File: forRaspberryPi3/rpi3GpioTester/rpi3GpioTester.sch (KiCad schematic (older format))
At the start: 59 parts, among them J1 Raspberry_Pi_2_3, J2 Conn_01x20_Male, J3 Conn_01x12_Male, SW12 SW_Push, SW13 SW_Push, SW16 SW_Push, SW17 SW_Push, SW18 SW_Push, SW19 SW_Push, SW20 SW_Push, SW21 SW_Push, SW22 SW_Push, SW23 SW_Push, SW24 SW_Push, SW25 SW_Push, SW26 SW_Push, SW27 SW_Push, SW4 SW_Push, SW5 SW_Push, SW6 SW_Push

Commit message: Add files via upload
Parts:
- added I2C3, I2C4, I2C5, I2C6: Conn_01x04_Female, Socket_Strips:Socket_Strip_Straight_1x04_Pitch2.54mm, symbol rpi3GpioTester-rescue:Conn_01x04_Female
- D12, D13, D16, D17, D18, D19, D20, D21, D22, D23, D24, D25, D26, D27, D4, D5, D6: symbol LED -> Device:LED
- I2C1, I2C2: symbol Conn_01x04_Female -> rpi3GpioTester-rescue:Conn_01x04_Female
- I2C7: renamed from I2C3; symbol Conn_01x04_Female -> rpi3GpioTester-rescue:Conn_01x04_Female
- I2C8: renamed from I2C4; symbol Conn_01x04_Female -> rpi3GpioTester-rescue:Conn_01x04_Female
- I2C_Grove1: symbol Conn_01x04 -> rpi3GpioTester-rescue:Conn_01x04
- J1: symbol Raspberry_Pi_2_3 -> rpi3GpioTester-rescue:Raspberry_Pi_2_3
- J2: symbol Conn_01x20_Male -> rpi3GpioTester-rescue:Conn_01x20_Male
- J3: symbol Conn_01x12_Male -> rpi3GpioTester-rescue:Conn_01x12_Male
- R12, R13, R16, R17, R18, R19, R20, R21, R22, R23, R24, R25, R26, R27, R4, R5, R6: symbol R -> Device:R
- SW12, SW13, SW16, SW17, SW18, SW19, SW20, SW21, SW22, SW23, SW24, SW25, SW26, SW27, SW4, SW5, SW6: symbol SW_Push -> rpi3GpioTester-rescue:SW_Push
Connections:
- net +3V3: now also I2C3.4 (Pin_4), I2C4.4 (Pin_4), I2C5.4 (Pin_4), I2C6.4 (Pin_4)
- net GND: now also I2C3.3 (Pin_3), I2C4.3 (Pin_3), I2C5.1 (Pin_1), I2C6.1 (Pin_1)
- net SCL: now also I2C3.2 (Pin_2), I2C4.2 (Pin_2), I2C5.2 (Pin_2), I2C6.2 (Pin_2)
- net SDA: now also I2C3.1 (Pin_1), I2C4.1 (Pin_1), I2C5.3 (Pin_3), I2C6.3 (Pin_3)
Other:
- moved on the sheet: I2C1, I2C2, I2C7, I2C8, I2C_Grove1

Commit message: rpi3GpioTester rev0.3
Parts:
- added I2C13, I2C14, I2C15, I2C16, I2C5, I2C6, I2C7, I2C8: Conn_01x04_Female, Socket_Strips:Socket_Strip_Straight_1x04_Pitch2.54mm, symbol rpi3GpioTester-rescue:Conn_01x04_Female
- added I2C_Grove2, I2C_Grove3, I2C_Grove4: Conn_01x04, Connectors:Grove_1x04, symbol rpi3GpioTester-rescue:Conn_01x04
- D12, D13, D16, D17, D18, D19, D20, D21, D22, D23, D24, D25, D26, D27, D4, D5, D6: symbol Device:LED -> rpi3GpioTester-rescue:LED-Device
- R12, R13, R16, R17, R18, R19, R20, R21, R22, R23, R24, R25, R26, R27, R4, R5, R6: symbol Device:R -> rpi3GpioTester-rescue:R-Device
- renumbered I2C6 to I2C10, I2C7 to I2C11, I2C8 to I2C12, I2C5 to I2C9
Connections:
- net +3V3: now also I2C13.4 (Pin_4), I2C14.4 (Pin_4), I2C15.4 (Pin_4), I2C16.4 (Pin_4), I2C5.4 (Pin_4), I2C6.4 (Pin_4), I2C7.4 (Pin_4), I2C8.4 (Pin_4), I2C_Grove2.3 (Pin_3), I2C_Grove3.3 (Pin_3), I2C_Grove4.3 (Pin_3)
- net GND: now also I2C13.1 (Pin_1), I2C14.1 (Pin_1), I2C15.1 (Pin_1), I2C16.1 (Pin_1), I2C5.3 (Pin_3), I2C6.3 (Pin_3), I2C7.3 (Pin_3), I2C8.3 (Pin_3), I2C_Grove2.4 (Pin_4), I2C_Grove3.4 (Pin_4), I2C_Grove4.4 (Pin_4)
- net SCL: now also I2C13.2 (Pin_2), I2C14.2 (Pin_2), I2C15.2 (Pin_2), I2C16.2 (Pin_2), I2C5.2 (Pin_2), I2C6.2 (Pin_2), I2C7.2 (Pin_2), I2C8.2 (Pin_2), I2C_Grove2.1 (Pin_1), I2C_Grove3.1 (Pin_1), I2C_Grove4.1 (Pin_1)
- net SDA: now also I2C13.3 (Pin_3), I2C14.3 (Pin_3), I2C15.3 (Pin_3), I2C16.3 (Pin_3), I2C5.1 (Pin_1), I2C6.1 (Pin_1), I2C7.1 (Pin_1), I2C8.1 (Pin_1), I2C_Grove2.2 (Pin_2), I2C_Grove3.2 (Pin_2), I2C_Grove4.2 (Pin_2)
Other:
- moved on the sheet: I2C1, I2C10, I2C11, I2C12, I2C2, I2C3, I2C4, I2C9, I2C_Grove1

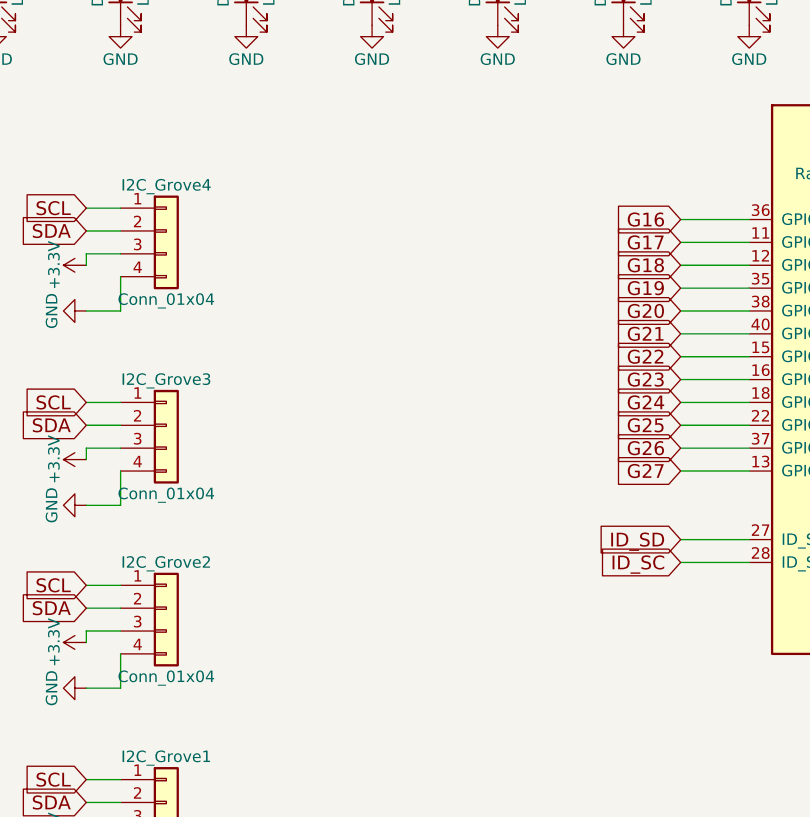
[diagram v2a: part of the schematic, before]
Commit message: Add I2C pull up pattern
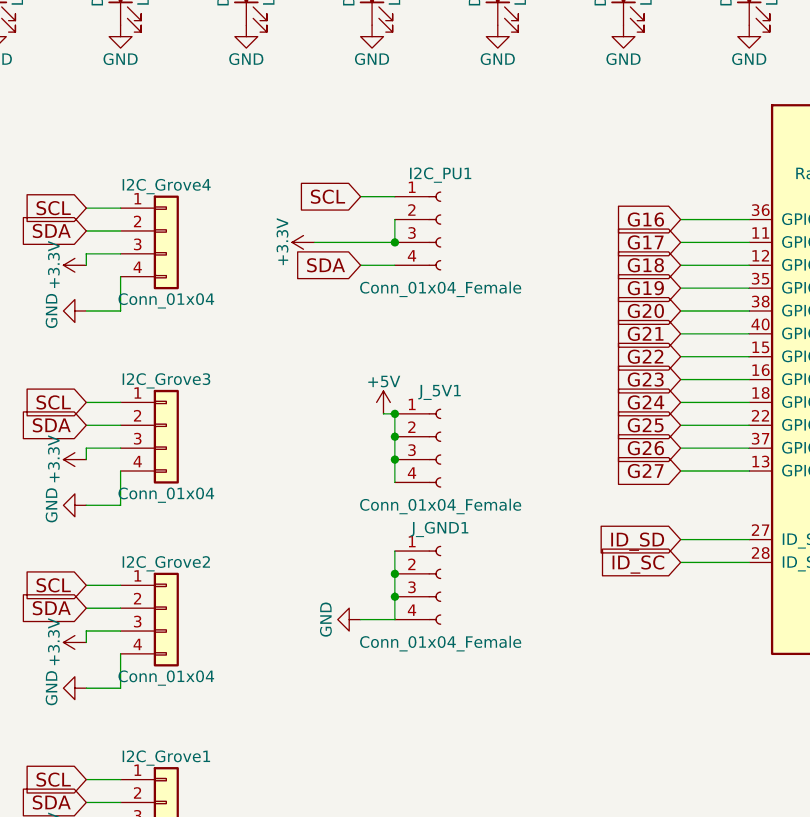
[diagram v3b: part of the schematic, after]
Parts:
- added I2C_PU1, J_5V1, J_GND1: Conn_01x04_Female, Socket_Strips:Socket_Strip_Straight_1x04_Pitch2.54mm, symbol rpi3GpioTester-rescue:Conn_01x04_Female
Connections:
- net +3V3: now also I2C_PU1.2 (Pin_2), I2C_PU1.3 (Pin_3)
- net +5V: now also J_5V1.1 (Pin_1), J_5V1.2 (Pin_2), J_5V1.3 (Pin_3), J_5V1.4 (Pin_4)
- net GND: now also J_GND1.1 (Pin_1), J_GND1.2 (Pin_2), J_GND1.3 (Pin_3), J_GND1.4 (Pin_4)
- net SCL: now also I2C_PU1.1 (Pin_1)
- net SDA: now also I2C_PU1.4 (Pin_4)
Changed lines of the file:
@@
 SDA
 $Comp
-L rpi3GpioTester-rescue:GND-power #PWR?
+L rpi3GpioTester-rescue:GND-power #PWR0109
 U 1 1 5DDAA191
 P 2450 4300
-F 0 "#PWR?" H 2450 4050 50  0001 C CNN
+F 0 "#PWR0109" H 2450 4050 50  0001 C CNN
 F 1 "GND" H 2450 4150 50  0000 C CNN
 F 2 "" H 2450 4300 50  0001 C CNN
@@
 $EndComp
 $Comp
-L rpi3GpioTester-rescue:+3.3V-power #PWR?
+L rpi3GpioTester-rescue:+3.3V-power #PWR0110
 U 1 1 5DDAA197
 P 2450 4500
-F 0 "#PWR?" H 2450 4350 50  0001 C CNN
+F 0 "#PWR0110" H 2450 4350 50  0001 C CNN
 F 1 "+3.3V" H 2450 4640 50  0000 C CNN
 F 2 "" H 2450 4500 50  0001 C CNN
@@
 SDA
 $Comp
-L rpi3GpioTester-rescue:GND-power #PWR?
+L rpi3GpioTester-rescue:GND-power #PWR0111
 U 1 1 5DDAA1A5
 P 2450 5050
-F 0 "#PWR?" H 2450 4800 50  0001 C CNN
+F 0 "#PWR0111" H 2450 4800 50  0001 C CNN
 F 1 "GND" H 2450 4900 50  0000 C CNN
 F 2 "" H 2450 5050 50  0001 C CNN
@@
 $EndComp
 $Comp
-L rpi3GpioTester-rescue:+3.3V-power #PWR?
+L rpi3GpioTester-rescue:+3.3V-power #PWR0112
 U 1 1 5DDAA1AB
 P 2450 5250
-F 0 "#PWR?" H 2450 5100 50  0001 C CNN
+F 0 "#PWR0112" H 2450 5100 50  0001 C CNN
 F 1 "+3.3V" H 2450 5390 50  0000 C CNN
 F 2 "" H 2450 5250 50  0001 C CNN
@@
 SDA
 $Comp
-L rpi3GpioTester-rescue:GND-power #PWR?
+L rpi3GpioTester-rescue:GND-power #PWR0113
 U 1 1 5DDAA1B9
 P 1000 6400
-F 0 "#PWR?" H 1000 6150 50  0001 C CNN
+F 0 "#PWR0113" H 1000 6150 50  0001 C CNN
 F 1 "GND" H 1000 6250 50  0000 C CNN
 F 2 "" H 1000 6400 50  0001 C CNN
@@
 $EndComp
 $Comp
-L rpi3GpioTester-rescue:+3.3V-power #PWR?
+L rpi3GpioTester-rescue:+3.3V-power #PWR0114
 U 1 1 5DDAA1BF
 P 1050 6850
-F 0 "#PWR?" H 1050 6700 50  0001 C CNN
+F 0 "#PWR0114" H 1050 6700 50  0001 C CNN
 F 1 "+3.3V" H 1050 6990 50  0000 C CNN
 F 2 "" H 1050 6850 50  0001 C CNN
@@
 SDA
 $Comp
-L rpi3GpioTester-rescue:GND-power #PWR?
+L rpi3GpioTester-rescue:GND-power #PWR0115
 U 1 1 5DDAA1CD
 P 1000 5650
-F 0 "#PWR?" H 1000 5400 50  0001 C CNN
+F 0 "#PWR0115" H 1000 5400 50  0001 C CNN
 F 1 "GND" H 1000 5500 50  0000 C CNN
 F 2 "" H 1000 5650 50  0001 C CNN
@@
 $EndComp
 $Comp
-L rpi3GpioTester-rescue:+3.3V-power #PWR?
+L rpi3GpioTester-rescue:+3.3V-power #PWR0116
 U 1 1 5DDAA1D3
 P 1050 6100
-F 0 "#PWR?" H 1050 5950 50  0001 C CNN
+F 0 "#PWR0116" H 1050 5950 50  0001 C CNN
 F 1 "+3.3V" H 1050 6240 50  0000 C CNN
 F 2 "" H 1050 6100 50  0001 C CNN
@@
 SDA
 $Comp
-L rpi3GpioTester-rescue:GND-power #PWR?
+L rpi3GpioTester-rescue:GND-power #PWR0117
 U 1 1 5DDAA1F9
 P 2450 5850
-F 0 "#PWR?" H 2450 5600 50  0001 C CNN
+F 0 "#PWR0117" H 2450 5600 50  0001 C CNN
 F 1 "GND" H 2450 5700 50  0000 C CNN
 F 2 "" H 2450 5850 50  0001 C CNN
@@
 $EndComp
 $Comp
-L rpi3GpioTester-rescue:+3.3V-power #PWR?
+L rpi3GpioTester-rescue:+3.3V-power #PWR0118
 U 1 1 5DDAA1FF
 P 2450 6050
-F 0 "#PWR?" H 2450 5900 50  0001 C CNN
+F 0 "#PWR0118" H 2450 5900 50  0001 C CNN
 F 1 "+3.3V" H 2450 6190 50  0000 C CNN
 F 2 "" H 2450 6050 50  0001 C CNN
@@
 SDA
 $Comp
-L rpi3GpioTester-rescue:GND-power #PWR?
+L rpi3GpioTester-rescue:GND-power #PWR0119
 U 1 1 5DDAA20D
 P 2450 6600
-F 0 "#PWR?" H 2450 6350 50  0001 C CNN
+F 0 "#PWR0119" H 2450 6350 50  0001 C CNN
 F 1 "GND" H 2450 6450 50  0000 C CNN
 F 2 "" H 2450 6600 50  0001 C CNN
@@
 $EndComp
 $Comp
-L rpi3GpioTester-rescue:+3.3V-power #PWR?
+L rpi3GpioTester-rescue:+3.3V-power #PWR0120
 U 1 1 5DDAA213
 P 2450 6800
-F 0 "#PWR?" H 2450 6650 50  0001 C CNN
+F 0 "#PWR0120" H 2450 6650 50  0001 C CNN
 F 1 "+3.3V" H 2450 6940 50  0000 C CNN
 F 2 "" H 2450 6800 50  0001 C CNN
@@
 SDA
 $Comp
-L rpi3GpioTester-rescue:GND-power #PWR?
+L rpi3GpioTester-rescue:GND-power #PWR0121
 U 1 1 5DDAA221
 P 1000 4800
-F 0 "#PWR?" H 1000 4550 50  0001 C CNN
+F 0 "#PWR0121" H 1000 4550 50  0001 C CNN
 F 1 "GND" H 1000 4650 50  0000 C CNN
 F 2 "" H 1000 4800 50  0001 C CNN
@@
 $EndComp
 $Comp
-L rpi3GpioTester-rescue:+3.3V-power #PWR?
+L rpi3GpioTester-rescue:+3.3V-power #PWR0122
 U 1 1 5DDAA227
 P 1050 5250
-F 0 "#PWR?" H 1050 5100 50  0001 C CNN
+F 0 "#PWR0122" H 1050 5100 50  0001 C CNN
 F 1 "+3.3V" H 1050 5390 50  0000 C CNN
 F 2 "" H 1050 5250 50  0001 C CNN
@@
 SDA
 $Comp
-L rpi3GpioTester-rescue:GND-power #PWR?
+L rpi3GpioTester-rescue:GND-power #PWR0123
 U 1 1 5DDAA235
 P 1000 4050
-F 0 "#PWR?" H 1000 3800 50  0001 C CNN
+F 0 "#PWR0123" H 1000 3800 50  0001 C CNN
 F 1 "GND" H 1000 3900 50  0000 C CNN
 F 2 "" H 1000 4050 50  0001 C CNN
@@
 $EndComp
 $Comp
-L rpi3GpioTester-rescue:+3.3V-power #PWR?
+L rpi3GpioTester-rescue:+3.3V-power #PWR0124
 U 1 1 5DDAA23B
 P 1050 4500
-F 0 "#PWR?" H 1050 4350 50  0001 C CNN
+F 0 "#PWR0124" H 1050 4350 50  0001 C CNN
 F 1 "+3.3V" H 1050 4640 50  0000 C CNN
 F 2 "" H 1050 4500 50  0001 C CNN
@@
 SDA
 $Comp
-L rpi3GpioTester-rescue:GND-power #PWR?
+L rpi3GpioTester-rescue:GND-power #PWR0125
 U 1 1 5DD88E0E
 P 5750 4700
-F 0 "#PWR?" H 5750 4450 50  0001 C CNN
+F 0 "#PWR0125" H 5750 4450 50  0001 C CNN
 F 1 "GND" H 5750 4550 50  0000 C CNN
 F 2 "" H 5750 4700 50  0001 C CNN
@@
 $EndComp
 $Comp
-L rpi3GpioTester-rescue:+3.3V-power #PWR?
+L rpi3GpioTester-rescue:+3.3V-power #PWR0126
 U 1 1 5DD88E14
 P 5750 4500
-F 0 "#PWR?" H 5750 4350 50  0001 C CNN
+F 0 "#PWR0126" H 5750 4350 50  0001 C CNN
 F 1 "+3.3V" H 5750 4640 50  0000 C CNN
 F 2 "" H 5750 4500 50  0001 C CNN
@@
 SDA
 $Comp
-L rpi3GpioTester-rescue:GND-power #PWR?
+L rpi3GpioTester-rescue:GND-power #PWR0127
 U 1 1 5DD9ED50
 P 5750 5550
-F 0 "#PWR?" H 5750 5300 50  0001 C CNN
+F 0 "#PWR0127" H 5750 5300 50  0001 C CNN
 F 1 "GND" H 5750 5400 50  0000 C CNN
 F 2 "" H 5750 5550 50  0001 C CNN
@@
 $EndComp
 $Comp
-L rpi3GpioTester-rescue:+3.3V-power #PWR?
+L rpi3GpioTester-rescue:+3.3V-power #PWR0128
 U 1 1 5DD9ED56
 P 5750 5350
-F 0 "#PWR?" H 5750 5200 50  0001 C CNN
+F 0 "#PWR0128" H 5750 5200 50  0001 C CNN
 F 1 "+3.3V" H 5750 5490 50  0000 C CNN
 F 2 "" H 5750 5350 50  0001 C CNN
@@
 SDA
 $Comp
-L rpi3GpioTester-rescue:GND-power #PWR?
+L rpi3GpioTester-rescue:GND-power #PWR0129
 U 1 1 5DDB603C
 P 5750 6350
-F 0 "#PWR?" H 5750 6100 50  0001 C CNN
+F 0 "#PWR0129" H 5750 6100 50  0001 C CNN
 F 1 "GND" H 5750 6200 50  0000 C CNN
 F 2 "" H 5750 6350 50  0001 C CNN
@@
 $EndComp
 $Comp
-L rpi3GpioTester-rescue:+3.3V-power #PWR?
+L rpi3GpioTester-rescue:+3.3V-power #PWR0130
 U 1 1 5DDB6042
 P 5750 6150
-F 0 "#PWR?" H 5750 6000 50  0001 C CNN
+F 0 "#PWR0130" H 5750 6000 50  0001 C CNN
 F 1 "+3.3V" H 5750 6290 50  0000 C CNN
 F 2 "" H 5750 6150 50  0001 C CNN
@@
 Wire Wire Line
 	5900 6350 5900 6200
+$Comp
+L rpi3GpioTester-rescue:Conn_01x04_Female I2C_PU1
+U 1 1 5DD8E5EE
+P 7300 4300
+F 0 "I2C_PU1" H 7300 4500 50  0000 C CNN
+F 1 "Conn_01x04_Female" H 7300 4000 50  0000 C CNN
+F 2 "Socket_Strips:Socket_Strip_Straight_1x04_Pitch2.54mm" H 7300 4300 50  0001 C CNN
+F 3 "" H 7300 4300 50  0001 C CNN
+	1    7300 4300
+	1    0    0    -1
+$EndComp
+Text GLabel 6950 4200 0    60   Input ~ 0
+SCL
+Text GLabel 6950 4500 0    60   Input ~ 0
+SDA
+$Comp
+L rpi3GpioTester-rescue:+3.3V-power #PWR0131
+U 1 1 5DD8E5FC
+P 6750 4400
+F 0 "#PWR0131" H 6750 4250 50  0001 C CNN
+F 1 "+3.3V" H 6750 4540 50  0000 C CNN
+F 2 "" H 6750 4400 50  0001 C CNN
+F 3 "" H 6750 4400 50  0001 C CNN
+	1    6750 4400
+	0    -1   -1   0
+$EndComp
+Wire Wire Line
+	6950 4500 7100 4500
+Wire Wire Line
+	6950 4200 7100 4200
+Wire Wire Line
+	7100 4300 7100 4400
+Connection ~ 7100 4400
+Wire Wire Line
+	6750 4400 7100 4400
+$Comp
+L rpi3GpioTester-rescue:Conn_01x04_Female J_5V1
+U 1 1 5DE85532
+P 7300 5250
+F 0 "J_5V1" H 7300 5450 50  0000 C CNN
+F 1 "Conn_01x04_Female" H 7300 4950 50  0000 C CNN
+F 2 "Socket_Strips:Socket_Strip_Straight_1x04_Pitch2.54mm" H 7300 5250 50  0001 C CNN
+F 3 "" H 7300 5250 50  0001 C CNN
+	1    7300 5250
+	1    0    0    -1
+$EndComp
+$Comp
+L rpi3GpioTester-rescue:+5V-power #PWR0132
+U 1 1 5DEBA508
+P 7050 5150
+F 0 "#PWR0132" H 7050 5000 50  0001 C CNN
+F 1 "+5V" H 7050 5290 50  0000 C CNN
+F 2 "" H 7050 5150 50  0001 C CNN
+F 3 "" H 7050 5150 50  0001 C CNN
+	1    7050 5150
+	1    0    0    -1
+$EndComp
+Wire Wire Line
+	7050 5150 7100 5150
+Wire Wire Line
+	7100 5150 7100 5250
+Connection ~ 7100 5150
+Connection ~ 7100 5250
+Wire Wire Line
+	7100 5250 7100 5350
+Connection ~ 7100 5350
+Wire Wire Line
+	7100 5350 7100 5450
+$Comp
+L rpi3GpioTester-rescue:Conn_01x04_Female J_GND1
+U 1 1 5DF0A267
+P 7300 5850
+F 0 "J_GND1" H 7300 6050 50  0000 C CNN
+F 1 "Conn_01x04_Female" H 7300 5550 50  0000 C CNN
+F 2 "Socket_Strips:Socket_Strip_Straight_1x04_Pitch2.54mm" H 7300 5850 50  0001 C CNN
+F 3 "" H 7300 5850 50  0001 C CNN
+	1    7300 5850
+	1    0    0    -1
+$EndComp
+Wire Wire Line
+	7100 5750 7100 5850
+Connection ~ 7100 5850
+Wire Wire Line
+	7100 5850 7100 5950
+Connection ~ 7100 5950
+Wire Wire Line
+	7100 5950 7100 6050
+$Comp
+L rpi3GpioTester-rescue:GND-power #PWR0133
+U 1 1 5DF3E28F
+P 6950 6050
+F 0 "#PWR0133" H 6950 5800 50  0001 C CNN
+F 1 "GND" H 6950 5900 50  0000 C CNN
+F 2 "" H 6950 6050 50  0001 C CNN
+F 3 "" H 6950 6050 50  0001 C CNN
+	1    6950 6050
+	0    1    1    0
+$EndComp
+Wire Wire Line
+	6950 6050 7100 6050
 $EndSCHEMATC
